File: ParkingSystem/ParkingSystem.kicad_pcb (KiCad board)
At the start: 2 copper layers, 43 parts, among them J1 PJ-002A, J2 0430450400, J3 Conn_ARM_JTAG_SWD_10, J4 Conn_01x04_Female, J5 0430450200, Q1 SSM3K333R,LF, Q2 SSM3K333R,LF, Q3 SSM3K333R,LF, Q4 SSM3K333R,LF, Q5 SSM3K333R,LF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

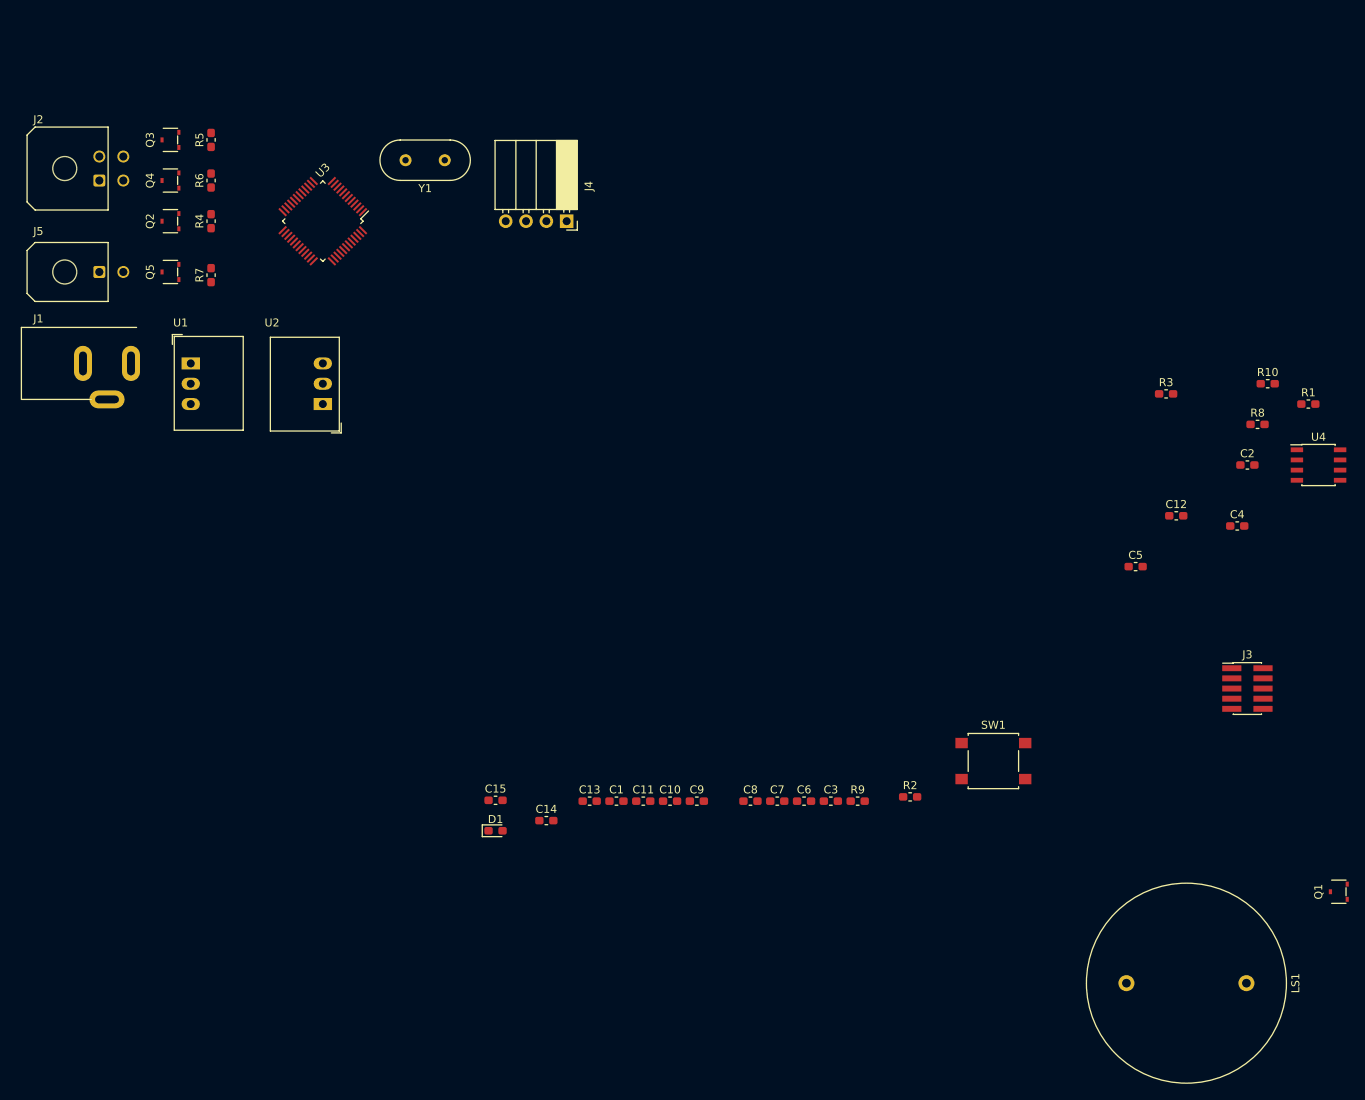
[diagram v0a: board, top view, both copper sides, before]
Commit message: Temporary part placement complete
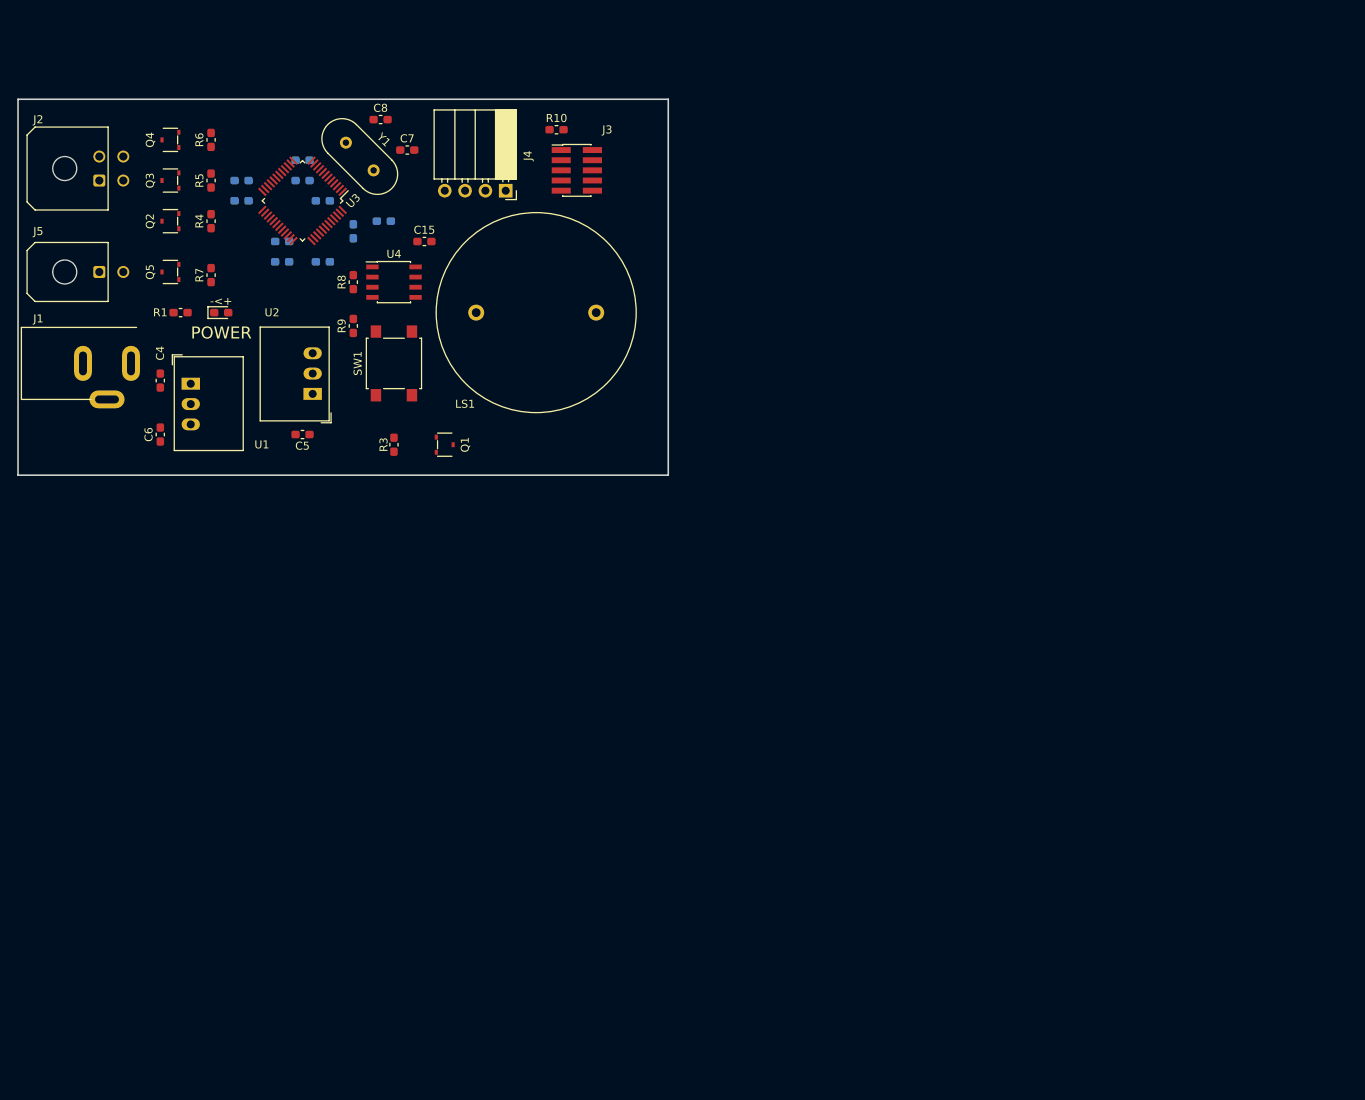
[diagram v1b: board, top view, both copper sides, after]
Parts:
- C1, C10, C11, C12, C13, C14, C2, C3, C9, R2: moved to B.Cu
- moved R1 141.4 mm to (88.9, 71.1), turned to 180 degrees
- moved C4 135.8 mm to (86.4, 79.6), turned to 270 degrees
- moved Q1 125.0 mm to (121.9, 87.6), turned to 270 degrees
- moved C2 123.3 mm to (101.6, 64.8), turned to 180 degrees
- moved C12 117.9 mm to (104.1, 52.1), turned to 180 degrees
- moved U4 117.8 mm to (115.6, 67.3)
- moved LS1 116.8 mm to (133.3, 71.1)
- moved R8 114.4 mm to (110.5, 67.3), turned to 90 degrees
- moved J3 105.9 mm to (138.4, 53.3)
- moved C5 105.4 mm to (104.1, 86.4), turned to 180 degrees
- moved R2 99.3 mm to (106.7, 64.8)
- moved C3 98.3 mm to (106.7, 57.1), turned to 180 degrees
- moved C8 96.9 mm to (113.9, 47.0)
- moved R3 96.7 mm to (115.6, 87.6), turned to 270 degrees
- moved R10 94.4 mm to (135.9, 48.3)
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- renumbered D1 to -<+
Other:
- board outline added: 81.3 x 47 mm
- board text added: "POWER"

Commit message: Move for better placement
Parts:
- removed -<+: LED, LED_SMD:LED_0603_1608Metric_Pad1.05x0.95mm_HandSolder
- added D1: LED, LED_SMD:LED_0603_1608Metric_Pad1.05x0.95mm_HandSolder, F.Cu at (94.0, 71.1)
- C14: moved to F.Cu
- moved J3 38.7 mm to (102.9, 68.6)
- moved R10 36.5 mm to (110.5, 74.5), turned to 90 degrees
- moved R8 35.8 mm to (144.8, 57.1), turned to 0 degrees
- moved C15 27.9 mm to (147.3, 62.2)
- moved C14 23.4 mm to (137.2, 54.6)
- moved C6 18.4 mm to (104.5, 88.9), turned to 180 degrees
- moved C5 17.8 mm to (86.4, 86.4), turned to 90 degrees
- moved R2 13.0 mm to (94.0, 62.2)
- moved Q2 10.2 mm to (87.6, 49.5)
- moved R4 10.2 mm to (92.7, 49.5)
- moved U4 5.24 mm to (114.3, 62.2)
- moved Q3 5.08 mm to (87.6, 59.7)
- moved Q4 5.08 mm to (87.6, 54.6)
- moved R5 5.08 mm to (92.7, 59.7)
- moved R6 5.08 mm to (92.7, 54.6)
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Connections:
- C15 pad 1: +5V -> +3V3
- U3 pad 45: Net-(U3-Pad45) -> /INDICATOR
- U4 pad 8: +5V -> +3V3

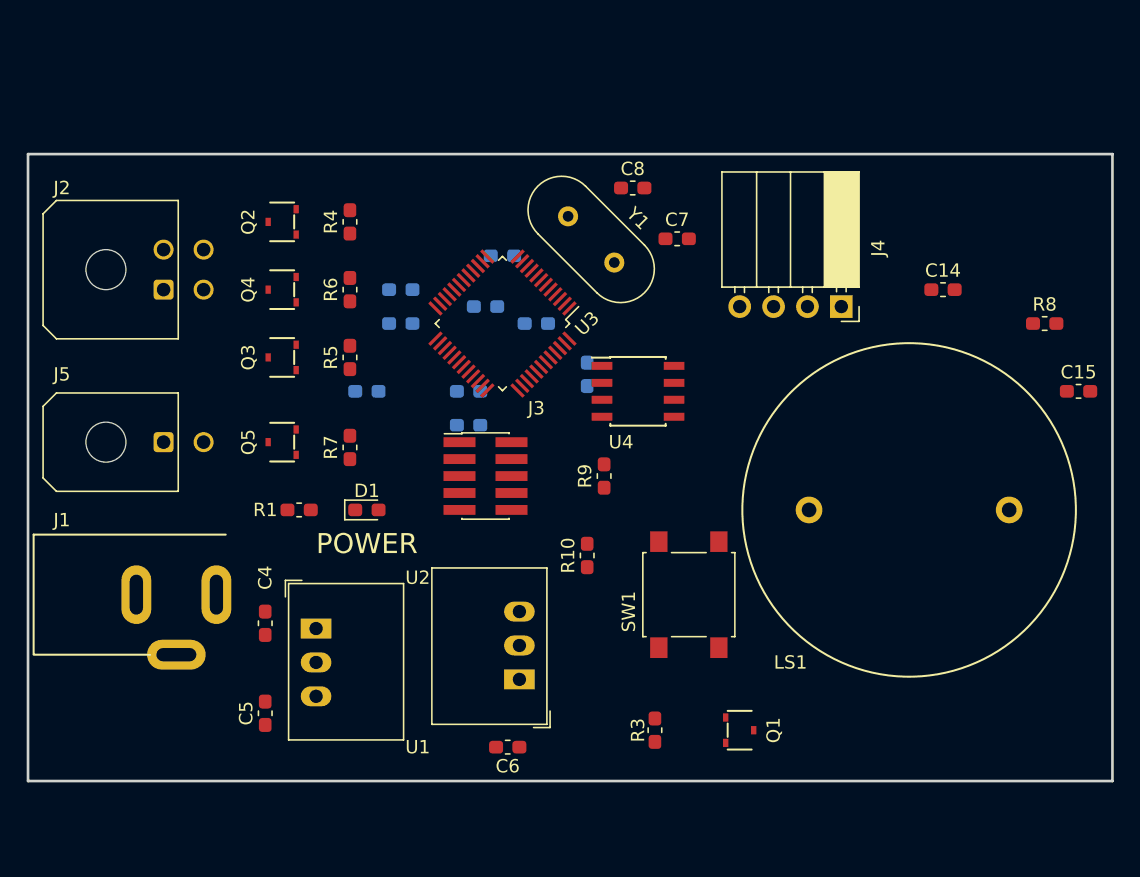
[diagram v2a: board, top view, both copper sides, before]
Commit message: Change MCU pin I/O lines and route
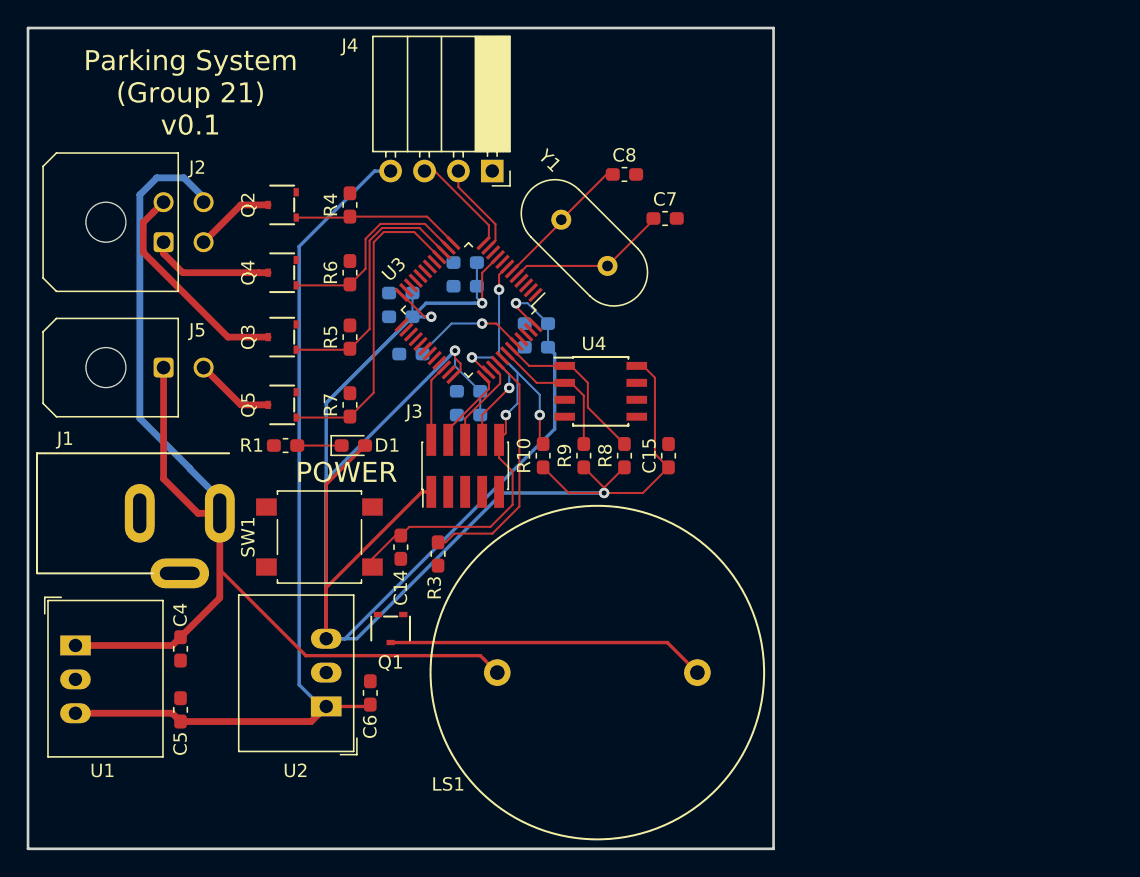
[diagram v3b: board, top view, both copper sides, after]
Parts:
- moved C14 45.0 mm to (96.5, 73.9), turned to 270 degrees
- moved R8 33.0 mm to (113.3, 67.1), turned to 90 degrees
- moved C15 31.1 mm to (116.6, 67.1), turned to 90 degrees
- moved J4 28.1 mm to (103.4, 45.7)
- moved SW1 28.0 mm to (90.4, 73.2), turned to 180 degrees
- moved Q1 27.2 mm to (95.8, 80.0), turned to 180 degrees
- moved LS1 26.4 mm to (111.3, 83.3)
- moved R3 20.9 mm to (99.3, 74.4)
- moved U1 18.1 mm to (72.1, 81.3)
- moved U2 14.6 mm to (90.9, 85.9)
- moved C6 11.1 mm to (94.2, 84.8), turned to 90 degrees
- moved R10 8.18 mm to (107.2, 67.1)
- moved C4 6.63 mm to (80.0, 81.5)
- moved C5 6.36 mm to (80.0, 86.1)
- moved J1 6.10 mm to (76.5, 71.4)
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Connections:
- U3 pad 10: /TRIG -> Net-(U3-Pad10)
- U3 pad 12: Net-(U3-Pad12) -> /TRIG
- U3 pad 13: Net-(U3-Pad13) -> /RED
- U3 pad 14: /BUZZER -> /BLUE
- U3 pad 15: /RED -> /GREEN
- U3 pad 16: Net-(U3-Pad16) -> /INDICATOR
- U3 pad 21: /BLUE -> Net-(U3-Pad21)
- U3 pad 22: /GREEN -> Net-(U3-Pad22)
- U3 pad 40: Net-(U3-Pad40) -> /BUZZER
- U3 pad 45: /INDICATOR -> Net-(U3-Pad45)
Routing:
- net +3V3: track 0.00 -> 205.7 mm, vias 0 -> 5
- net +12V: track 0.00 -> 93.1 mm
- net +5V: track 0.00 -> 67.6 mm
- net /RESET: track 0.00 -> 40.6 mm, vias 0 -> 3
- net /BUZ_POWER: track 0.00 -> 23.9 mm
- net /INDICATOR: track 0.00 -> 23.9 mm
- net /GREEN: track 0.00 -> 19.5 mm
- net /BUZZER: track 0.00 -> 18.6 mm
- net /G_POWER: track 0.00 -> 16.4 mm
- net /BLUE: track 0.00 -> 15.4 mm
- net /RED: track 0.00 -> 12.6 mm
- net /I2C1_SDA: track 0.00 -> 12.5 mm
- net Net-(C7-Pad1): track 0.00 -> 12.1 mm
- net /TDI: track 0.00 -> 10.8 mm, vias 0 -> 2
- net /I2C1_SCL: track 0.00 -> 10.7 mm
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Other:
- board size 81.3 x 47 mm -> 55.9 x 61.5 mm
- board text added: "Parking System (Group 21) v0.1"

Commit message: Preliminary Layout Complete
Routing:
- net /BUZZER: track 18.6 -> 25.1 mm
- net GND: vias 0 -> 7
- added copper zone on B.Cu, net GND
- added copper zone on F.Cu, net GND
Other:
- board text added: "Designed by: Chathula Adikary"
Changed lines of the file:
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@@
   (general
     (thickness 1.6)
-    (drawings 6)
-    (tracks 220)
+    (drawings 7)
+    (tracks 230)
     (zones 0)
     (modules 43)
@@
     (user_trace_width 0.508)
     (trace_clearance 0.1524)
-    (zone_clearance 0.508)
+    (zone_clearance 0.1778)
     (zone_45_only no)
     (trace_min 0.1524)
@@
     )
   )
+  (gr_text "Designed by: Chathula Adikary" (at 121.92 55.118 90) (layer F.SilkS)
+    (effects (font (size 1.5 1.5) (thickness 0.3)))
+  )
   (gr_text "Parking System \n(Group 21)\nv0.1" (at 80.772 39.878) (layer F.SilkS)
     (effects (font (size 1.5 1.5) (thickness 0.3)))
@@
   (segment (start 114.667 69.85) (end 116.586 67.931) (width 0.1524) (layer F.Cu) (net 1))
   (segment (start 111.76 69.85) (end 114.667 69.85) (width 0.1524) (layer F.Cu) (net 1))
+  (via (at 82.804 79.756) (size 0.7874) (drill 0.381) (layers F.Cu B.Cu) (net 2))
+  (via (at 83.566 78.74) (size 0.7874) (drill 0.381) (layers F.Cu B.Cu) (net 2))
+  (via (at 81.28 77.978) (size 0.7874) (drill 0.381) (layers F.Cu B.Cu) (net 2))
+  (via (at 91.694 70.612) (size 0.7874) (drill 0.381) (layers F.Cu B.Cu) (net 2))
+  (via (at 91.694 71.882) (size 0.7874) (drill 0.381) (layers F.Cu B.Cu) (net 2))
+  (via (at 90.17 71.882) (size 0.7874) (drill 0.381) (layers F.Cu B.Cu) (net 2))
+  (via (at 90.17 73.152) (size 0.7874) (drill 0.381) (layers F.Cu B.Cu) (net 2))
   (segment (start 81.326 71.374) (end 82.954 71.374) (width 0.508) (layer F.Cu) (net 3))
   (segment (start 78.74 68.788) (end 81.326 71.374) (width 0.508) (layer F.Cu) (net 3))
@@
   (segment (start 103.792031 60.093798) (end 105.41 61.711767) (width 0.1524) (layer F.Cu) (net 22))
   (segment (start 105.41 61.711767) (end 105.41 70.866) (width 0.1524) (layer F.Cu) (net 22))
+  (segment (start 96.708 76.52) (end 96.708 78.96) (width 0.1524) (layer F.Cu) (net 22))
+  (segment (start 99.314 73.547) (end 99.314 73.914) (width 0.1524) (layer F.Cu) (net 22))
+  (segment (start 99.314 73.914) (end 96.708 76.52) (width 0.1524) (layer F.Cu) (net 22))
   (segment (start 98.490087 49.135) (end 100.468629 51.113542) (width 0.1524) (layer F.Cu) (net 23))
   (segment (start 92.71 49.135) (end 98.490087 49.135) (width 0.1524) (layer F.Cu) (net 23))
@@
   (segment (start 110.236 62.55) (end 109.281 61.595) (width 0.1524) (layer F.Cu) (net 29))
   (segment (start 110.236 66.181) (end 110.236 62.55) (width 0.1524) (layer F.Cu) (net 29))
+  (zone (net 2) (net_name GND) (layer F.Cu) (hatch edge 0.508)
+    (connect_pads (clearance 0.1778))
+    (min_thickness 0.1778)
+    (fill yes (arc_segments 16) (thermal_gap 0.508) (thermal_bridge_width 0.508))
+    (polygon
+      (pts
+        (xy 68.326 96.774) (xy 68.326 34.798) (xy 124.714 34.798) (xy 124.714 96.774)
+      )
+    )
+  )
+  (zone (net 2) (net_name GND) (layer B.Cu) (hatch edge 0.508)
+    (connect_pads (clearance 0.1778))
+    (min_thickness 0.1778)
+    (fill yes (arc_segments 16) (thermal_gap 0.508) (thermal_bridge_width 0.508))
+    (polygon
+      (pts
+        (xy 68.326 96.774) (xy 68.326 34.798) (xy 124.714 34.798) (xy 124.714 96.774)
+      )
+    )
+  )
 )
